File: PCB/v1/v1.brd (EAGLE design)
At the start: 115.2 x 97.8 mm, 55 parts, among them U2 AT24C512C-SHD-B

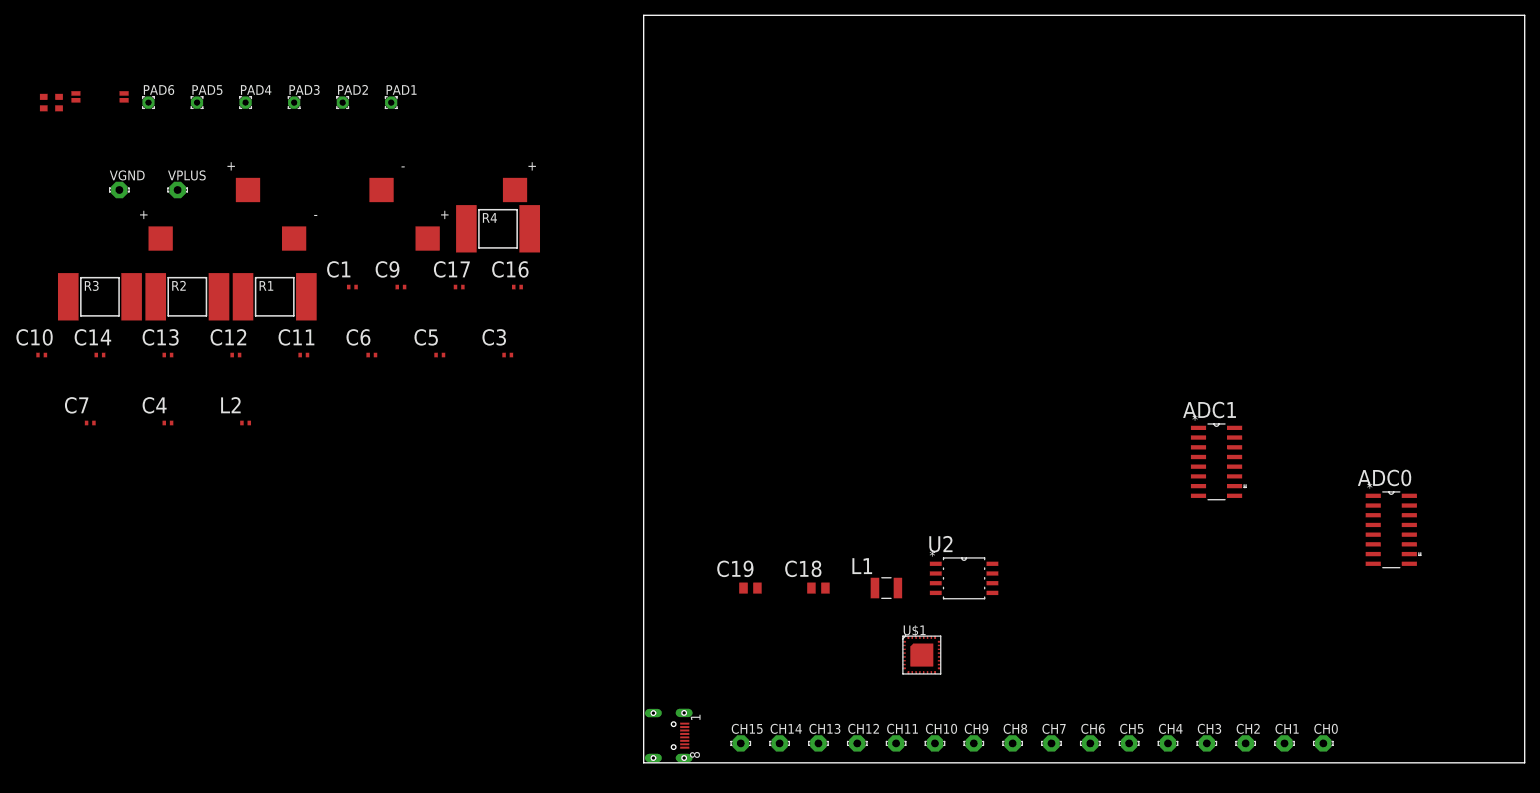
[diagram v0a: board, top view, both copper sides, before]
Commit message: using project to link schem and board. Need RF still
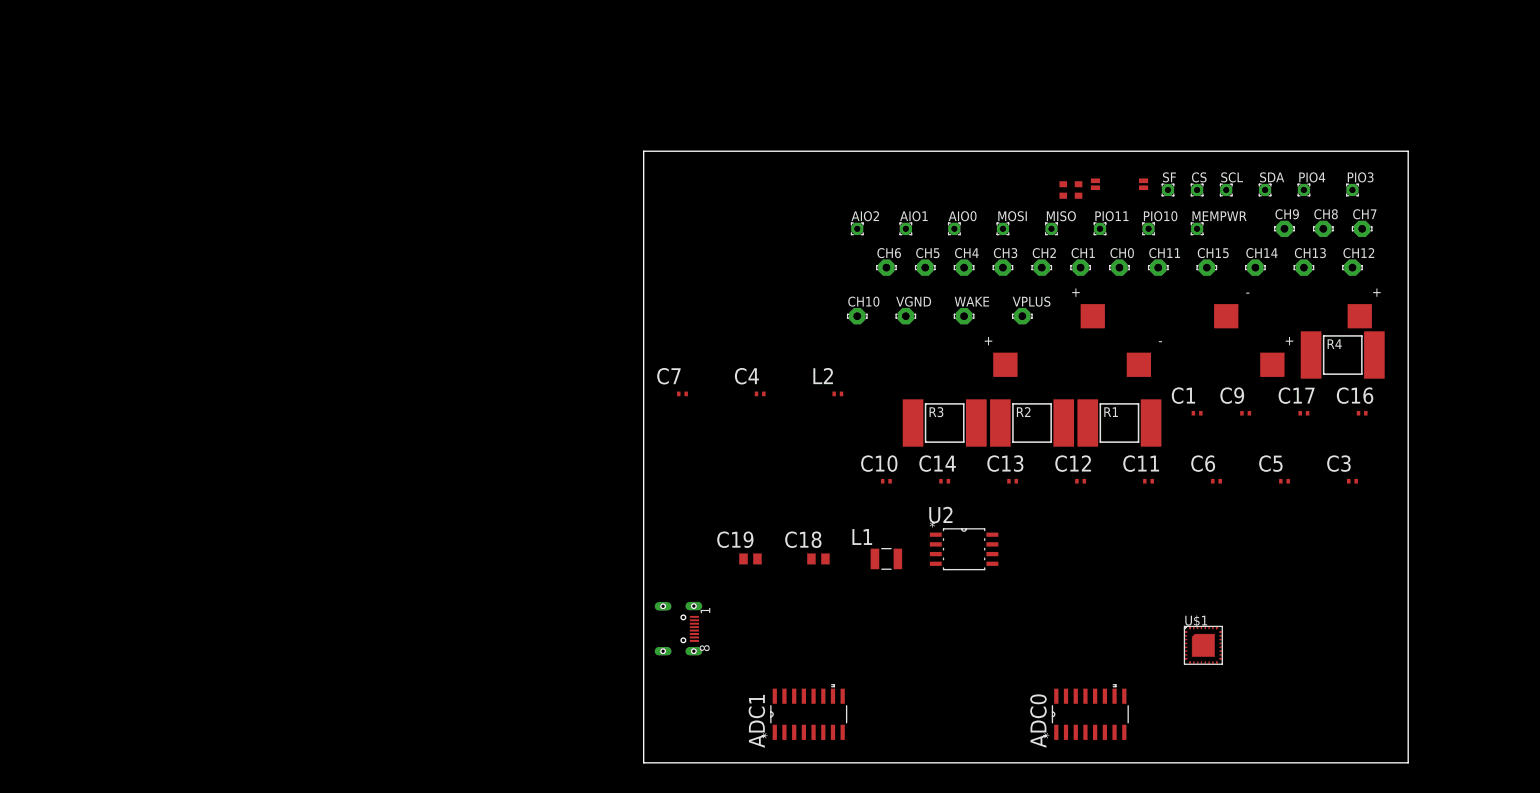
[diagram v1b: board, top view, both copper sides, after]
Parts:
- removed PAD1, PAD2, PAD3, PAD4, PAD5, PAD6: (no value), wirepad:1,6/0,8
- added AIO0, AIO1, AIO2, CS, MEMPWR, MISO, MOSI, PIO10, PIO11, PIO3, PIO4, SCL, SDA, SF: (no value), wirepad:1,6/0,8
- added WAKE: Vrail, solpad:LSP10
- moved U$3 133.8 mm to (55.9, 74.9)
- moved U$4 133.8 mm to (59.7, 74.9)
- moved C1 111.7 mm to (72.4, 45.7)
- moved C11 111.7 mm to (66.0, 36.8)
- moved C12 111.7 mm to (57.1, 36.8)
- moved C14 111.7 mm to (39.4, 36.8)
- moved C16 111.7 mm to (94.0, 45.7)
- moved C6 111.7 mm to (74.9, 36.8)
- moved R3 111.7 mm to (39.4, 44.5)
- moved U$6 111.7 mm to (76.2, 58.4)
- moved VPLUS 111.7 mm to (49.5, 58.4)
- moved C10 111.7 mm to (31.8, 36.8)
- moved C13 111.7 mm to (48.3, 36.8)
- moved C17 111.7 mm to (86.4, 45.7)
- moved C3 111.7 mm to (92.7, 36.8)
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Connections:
- removed net N$17: U$1.I2C_SDA, U2.5
- removed net N$43: PAD4.1, U$1.PIO[3]/SF_DIN
- new net N$49: U$1.WAKE, WAKE.MP
- new net N$50: MOSI.1, U$1.PIO[7]/DEBUG_MOSI, U$2.2
- new net N$51: SF.1, U$1.PIO[5]/DEBUG_CLK, U$2.3
- net GND: no longer U$1.WAKE
- net N$18: now also MISO.1, U$1.PIO[8]/DEBUG_MISO, U$2.5; no longer U$1.I2C_SCL, U2.6
- net N$21: now also SCL.1, U$1.I2C_SCL, U2.6; no longer U$1.PIO[5]/DEBUG_CLK, U$2.3
- net N$22: now also SDA.1, U$1.I2C_SDA, U2.5; no longer U$1.PIO[8]/DEBUG_MISO, U$2.5
- net N$23: now also PIO3.1, U$1.PIO[3]/SF_DIN; no longer U$1.PIO[7]/DEBUG_MOSI, U$2.2
- net N$25: now also PIO4.1
- net N$31: now also CS.1
- net N$33: now also AIO2.1; no longer PAD1.1
- net N$41: now also AIO1.1; no longer PAD2.1
- net N$42: now also AIO0.1; no longer PAD3.1
- net N$44: now also PIO10.1; no longer PAD5.1
- net N$46: now also MEMPWR.1
- net N$47: now also PIO11.1; no longer PAD6.1
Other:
- board size 115.2 x 97.8 mm -> 100 x 80 mm

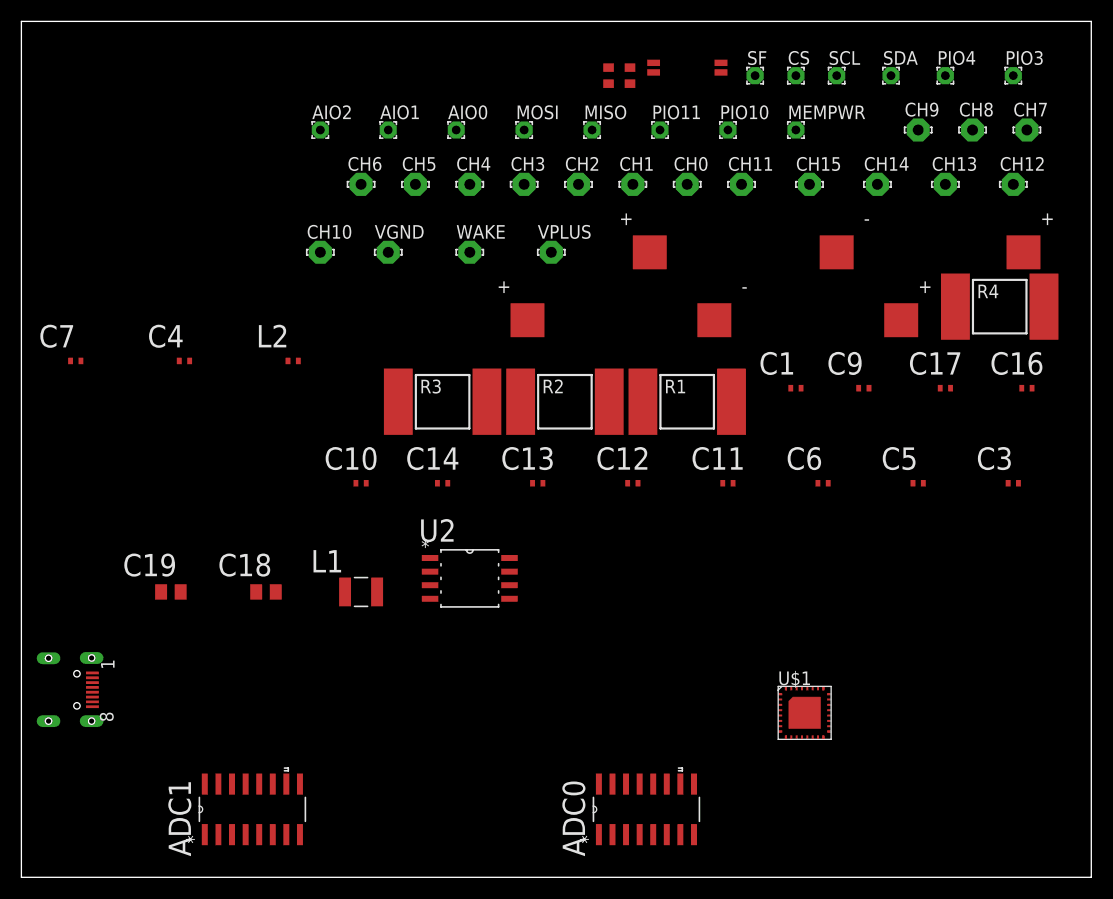
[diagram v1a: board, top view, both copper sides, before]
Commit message: need to do the RF and track up
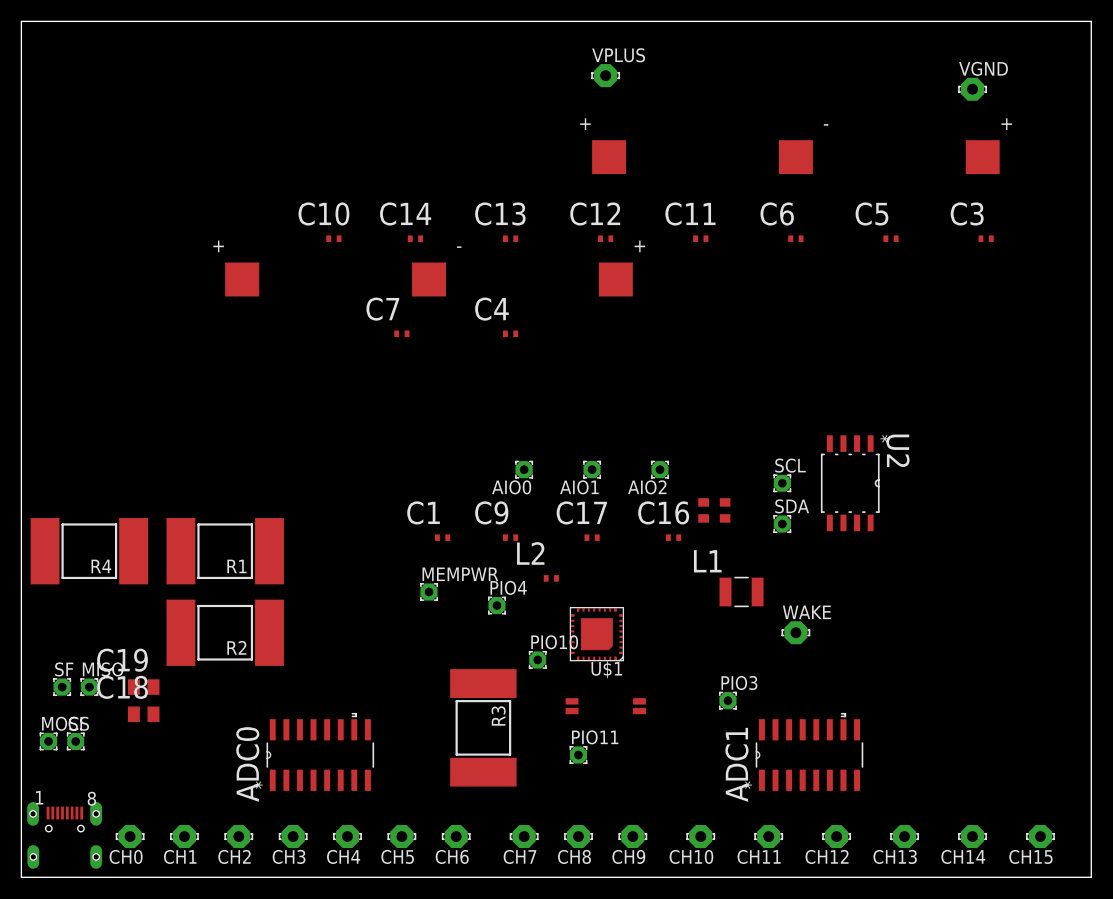
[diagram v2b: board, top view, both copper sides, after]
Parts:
- moved CS 91.7 mm to (5.08, 12.7)
- moved R4 88.1 mm to (6.35, 30.5), turned to 180 degrees
- moved SF 86.4 mm to (3.81, 17.8)
- moved CH7 81.1 mm to (47.0, 3.81), turned to 180 degrees
- moved CH0 80.2 mm to (10.2, 3.81), turned to 180 degrees
- moved CH8 75.6 mm to (52.1, 3.81), turned to 180 degrees
- moved CH1 74.0 mm to (15.2, 3.81), turned to 180 degrees
- moved MOSI 72.4 mm to (2.54, 12.7)
- moved CH9 71.2 mm to (57.1, 3.81), turned to 180 degrees
- moved MISO 70.1 mm to (6.35, 17.8)
- moved CH2 68.7 mm to (20.3, 3.81), turned to 180 degrees
- moved CH10 65.2 mm to (63.5, 3.81), turned to 180 degrees
- moved PIO4 64.9 mm to (44.5, 25.4)
- moved CH15 64.7 mm to (95.2, 3.81), turned to 180 degrees
- moved CH3 64.7 mm to (25.4, 3.81), turned to 180 degrees
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
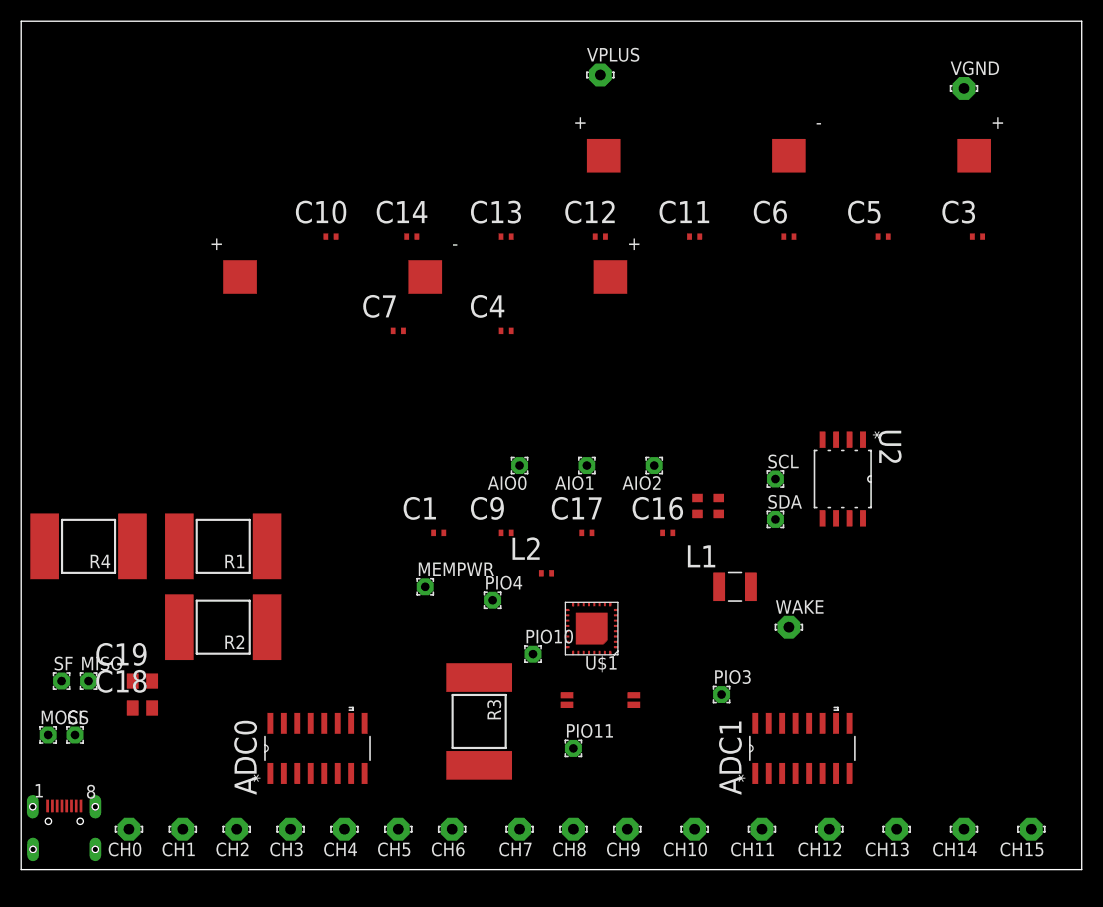
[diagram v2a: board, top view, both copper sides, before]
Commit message: corrected battery, still need RF. laying out zzzz
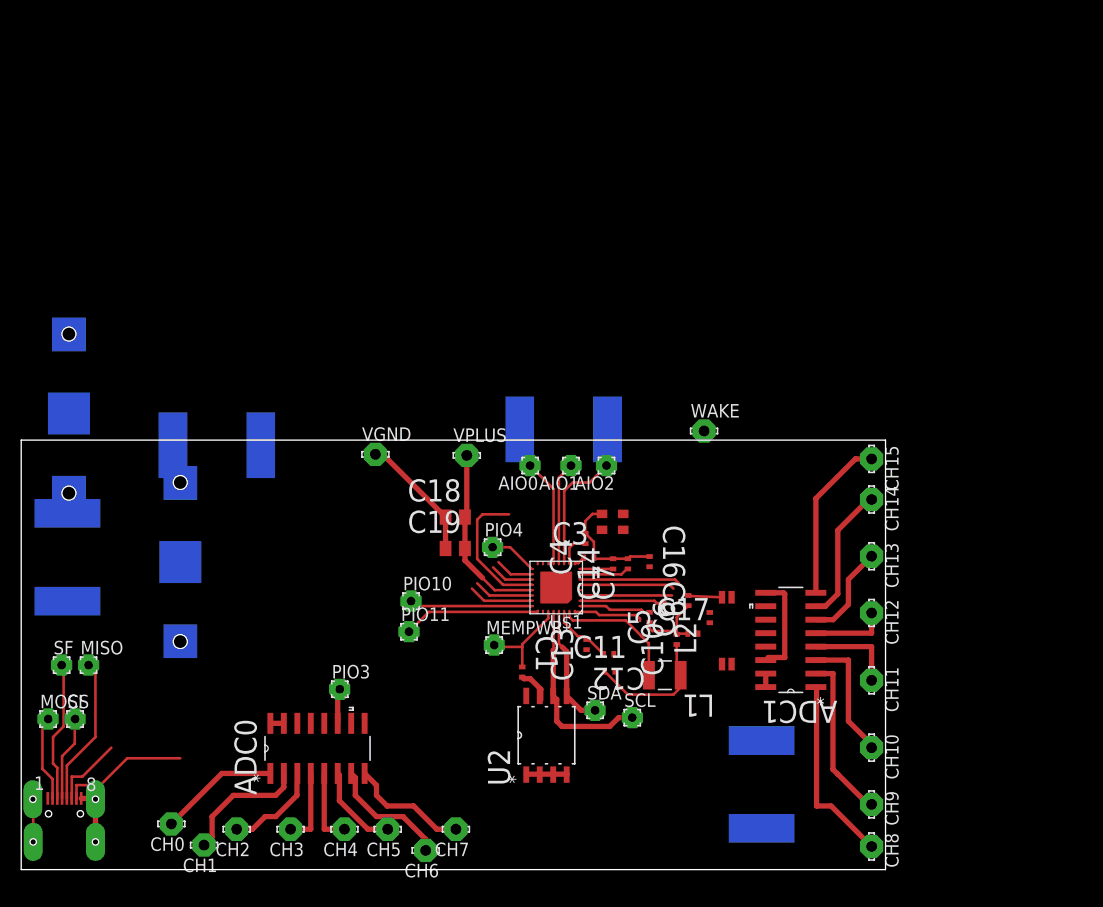
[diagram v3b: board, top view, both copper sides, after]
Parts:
- moved U$5 72.1 mm to (4.50, 43.0), flipped to the bottom, turned to 270 degrees
- moved VGND 65.3 mm to (33.4, 39.2)
- moved C10 50.1 mm to (61.8, 21.7), turned to 90 degrees
- moved C3 47.5 mm to (53.5, 29.4)
- moved R4 46.1 mm to (51.1, 41.5), flipped to the bottom, turned to 0 degrees
- moved C11 41.8 mm to (55.5, 18.7)
- moved C5 40.7 mm to (60.6, 24.6), turned to 90 degrees
- moved C12 39.4 mm to (55.4, 20.3), turned to 180 degrees
- moved C13 39.2 mm to (53.3, 21.2), turned to 90 degrees
- moved CH15 38.0 mm to (80.2, 38.7), turned to 270 degrees
- moved VPLUS 38.0 mm to (42.0, 39.1)
- moved U2 36.9 mm to (49.5, 12.7), turned to 90 degrees
- moved C14 36.2 mm to (55.8, 28.8), turned to 90 degrees
- moved PIO3 36.0 mm to (30.0, 17.0)
- moved C6 35.6 mm to (62.9, 25.4), turned to 90 degrees
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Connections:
- new net N$43: C7.1, U$1.RF
- net GND: no longer C7.1, U$1.RF
- net N$26: now also U$4.4
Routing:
- net GND: track 0.00 -> 62.9 mm
- net N$34: track 0.00 -> 24.1 mm
- net N$39: track 0.00 -> 22.0 mm
- net N$50: track 0.00 -> 21.2 mm
- net N$18: track 0.00 -> 19.8 mm
- net N$21: track 0.00 -> 18.2 mm
- net N$16: track 0.00 -> 18.0 mm
- net N$51: track 0.00 -> 16.9 mm
- net N$9: track 0.00 -> 15.7 mm
- net N$15: track 0.00 -> 15.7 mm
- net N$28: track 0.00 -> 14.8 mm
- net N$47: track 0.00 -> 12.9 mm
- net N$10: track 0.00 -> 12.8 mm
- net N$14: track 0.00 -> 12.2 mm
- net N$7: track 0.00 -> 12.2 mm
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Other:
- board size 100 x 80 mm -> 81.5 x 40.5 mm

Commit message: push to work from main pc
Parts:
- removed R1, R2, R3, R4: (no value), resistor-shunt:BVS
- added R5, R6, R7, R8: (no value), eagle-ltspice:R1206
- moved CH9 83.8 mm to (1.81, 35.9), turned to 90 degrees
- moved CH8 80.9 mm to (6.81, 36.3), turned to 90 degrees
- moved CH15 80.9 mm to (1.81, 18.8), turned to 90 degrees
- moved CH11 79.4 mm to (1.81, 30.6), turned to 90 degrees
- moved CH10 79.0 mm to (4.31, 33.5), turned to 90 degrees
- moved CH13 78.5 mm to (1.81, 24.9), turned to 90 degrees
- moved CH14 77.4 mm to (3.81, 22.1), turned to 90 degrees
- moved CH12 76.5 mm to (3.81, 27.8), turned to 90 degrees
- moved ADC1 62.9 mm to (9.93, 27.3), turned to 0 degrees
- moved U$5 52.9 mm to (45.0, 9.00), turned to 90 degrees
- moved U$6 30.0 mm to (45.0, 29.5), turned to 90 degrees
- moved WAKE 28.4 mm to (36.4, 36.4)
- moved L2 27.3 mm to (37.7, 21.4), turned to 180 degrees
- moved U$4 25.1 mm to (40.8, 23.1)
- moved C16 24.0 mm to (35.2, 28.5)
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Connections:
- net N$20: now also R7.1; no longer R1.2
- net N$36: now also R6.1; no longer R2.2
- net N$37: now also R7.2; no longer R1.1
- net N$38: now also R6.2; no longer R2.1
- net N$40: now also R8.1; no longer R4.2
- net N$45: now also R5.1; no longer R3.1
- net VDD: now also R5.2, R8.2; no longer R3.2, R4.1
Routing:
- net N$25: track 4.55 -> 49.4 mm
- net N$37: track 0.00 -> 33.6 mm
- net N$21: track 18.2 -> 47.1 mm
- net N$22: track 11.5 -> 39.5 mm
- net N$23: track 3.30 -> 28.5 mm
- net GND: track 62.9 -> 39.4 mm
- net N$49: track 0.00 -> 23.1 mm
- net N$16: track 18.0 -> 0.00 mm
- net N$48: track 0.00 -> 17.7 mm
- net N$9: track 15.7 -> 0.00 mm
- net N$15: track 15.7 -> 0.00 mm
- net N$45: track 0.00 -> 15.6 mm
- net N$10: track 12.8 -> 0.00 mm
- net N$14: track 12.2 -> 0.00 mm
- net N$18: track 19.8 -> 31.6 mm
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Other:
- board size 81.5 x 40.5 mm -> 53 x 38.5 mm

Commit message: takes its time
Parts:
- removed PIO10, PIO11: (no value), wirepad:1,6/0,8
- moved R8 14.2 mm to (4.17, 10.4)
- moved MOSI 8.20 mm to (7.54, 20.7)
- moved R5 6.02 mm to (18.0, 15.0), turned to 270 degrees
- moved C18 4.77 mm to (14.1, 37.6)
- moved C19 4.04 mm to (15.3, 35.2)
- moved C7 2.55 mm to (31.3, 26.1), turned to 0 degrees
- moved ADC1 2.00 mm to (9.93, 29.3)
- moved C14 1.80 mm to (31.3, 28.3)
- moved R6 1.50 mm to (12.0, 10.0)
- moved R7 1.50 mm to (12.0, 13.0)
- moved CH8 1.17 mm to (6.18, 37.3), turned to 180 degrees
- moved CH15 1.00 mm to (1.81, 19.8)
- moved VPLUS 0.67 mm to (17.9, 36.7)
- moved C3 0.50 mm to (30.0, 27.9)
- moved VGND 0.50 mm to (9.90, 36.7)
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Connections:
- removed net N$42: PIO10.1, U$1.PIO[10]
- removed net N$47: PIO11.1, U$1.PIO[11]
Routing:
- net N$21: track 47.1 -> 134.0 mm
- net N$22: track 39.5 -> 113.6 mm
- net VDD: track 2.56 -> 51.2 mm, vias 0 -> 1
- net N$25: track 49.4 -> 8.09 mm
- net N$50: track 12.6 -> 39.6 mm, vias 0 -> 1
- net N$38: track 9.46 -> 34.4 mm
- net N$31: track 12.6 -> 32.5 mm
- net N$34: track 18.7 -> 33.4 mm, vias 0 -> 1
- net N$37: track 33.6 -> 44.2 mm, vias 0 -> 1
- net N$40: track 8.90 -> 19.3 mm
- net N$23: track 28.5 -> 18.7 mm
- net N$51: track 25.7 -> 34.3 mm
- net N$42: track 6.24 -> 0.00 mm, vias 0 -> 1
- net N$45: track 15.6 -> 10.4 mm
- net N$47: track 3.94 -> 0.00 mm, vias 0 -> 1
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- added copper zone on layer 1, net GND
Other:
- board size 53 x 38.5 mm -> 53 x 39.2 mm

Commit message: getting there
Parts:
- moved C16 10.1 mm to (38.5, 19.0), turned to 180 degrees
- moved C11 7.31 mm to (38.7, 13.8), turned to 270 degrees
- moved C10 3.91 mm to (40.1, 16.2)
- moved L2 3.00 mm to (40.6, 21.1)
- moved C12 2.08 mm to (32.7, 20.2), turned to 90 degrees
- moved C13 2.02 mm to (31.6, 20.2)
- moved CH14 0.90 mm to (3.31, 22.9)
- moved C6 0.88 mm to (39.8, 24.1), turned to 270 degrees
- moved C17 0.79 mm to (40.6, 20.0)
- moved L1 0.79 mm to (36.9, 16.6)
- moved C9 0.31 mm to (36.0, 22.0), turned to 90 degrees
- moved CH15 0.25 mm to (1.56, 19.8)
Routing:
- net GND: track 37.1 -> 118.8 mm, vias 0 -> 4
- net N$34: track 33.4 -> 93.1 mm, vias 1 -> 2
- net N$25: track 8.09 -> 33.4 mm, vias 0 -> 1
- net N$23: track 18.7 -> 39.4 mm, vias 0 -> 1
- net N$28: track 14.2 -> 32.5 mm, vias 0 -> 2
- net N$39: track 23.7 -> 37.8 mm, vias 0 -> 2
- net N$24: track 2.71 -> 16.1 mm, vias 0 -> 2
- net N$38: track 34.4 -> 46.7 mm, vias 0 -> 1
- net N$22: track 113.6 -> 123.2 mm, vias 0 -> 1
- net N$21: track 134.0 -> 143.0 mm, vias 0 -> 1
- net N$15: track 0.00 -> 8.18 mm
- net N$9: track 0.00 -> 8.13 mm
- net N$11: track 0.00 -> 6.79 mm
- net N$13: track 0.00 -> 6.04 mm
- net N$10: track 0.00 -> 5.94 mm
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- added copper zone on layer 16, net GND
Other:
- board size 53 x 39.2 mm -> 53 x 39 mm
